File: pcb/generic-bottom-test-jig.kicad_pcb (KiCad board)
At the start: 2 copper layers, 88.5 x 56.8 mm, 47 parts, among them CON1 BARREL_JACK, P1 CONN_01X06, P10 CONN_01X01, P11 CONN_01X01, P2 CONN_02X25, P3 CONN_01X04, P4 CONN_02X25, P5 CONN_01X16, P6 CONN_02X10, P7 CONN_01X01, P8 CONN_01X16, P9 CONN_01X01, Q1 Q_NMOS_GSD, SW1 Switch_SPDT_x2, SW2 SPST, U1 STMPS2151, U2 TLV70233DBV, U3 74LS257

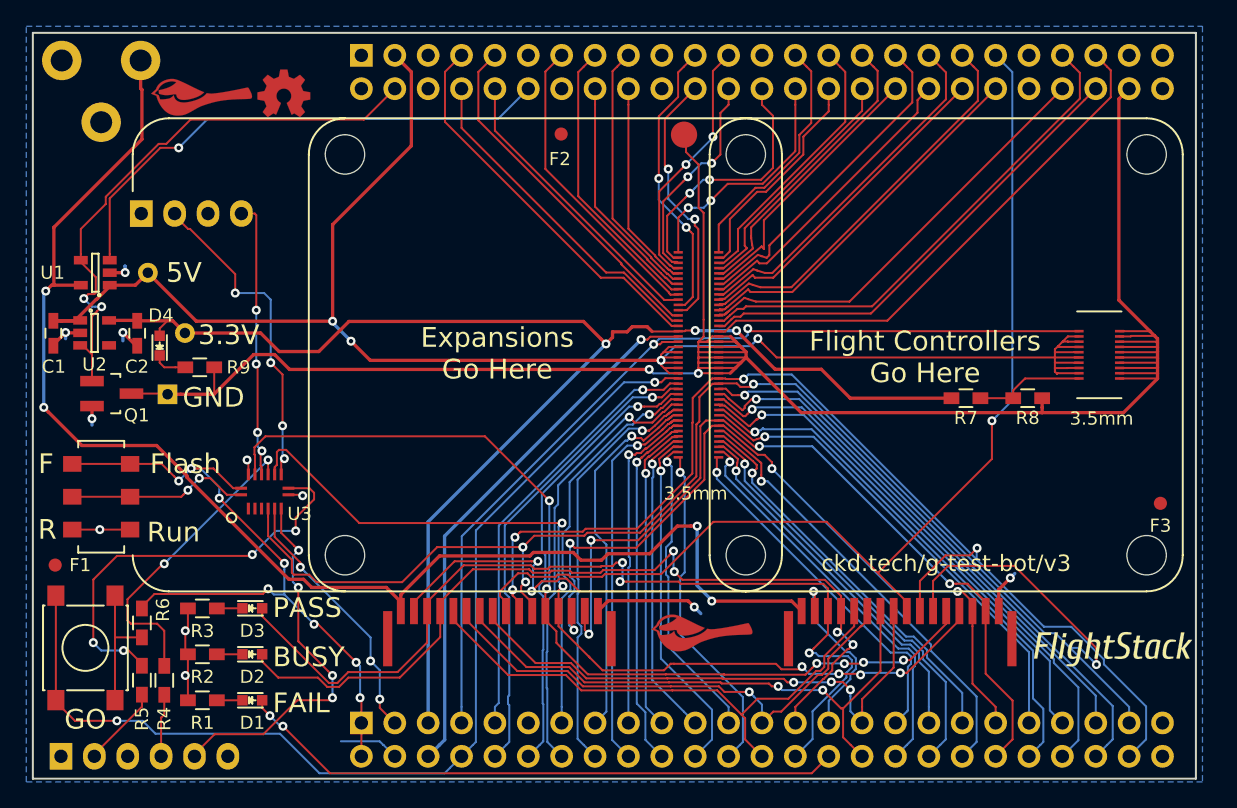
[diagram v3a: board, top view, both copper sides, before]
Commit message: Rebrand everything to Polystack and increment versions.
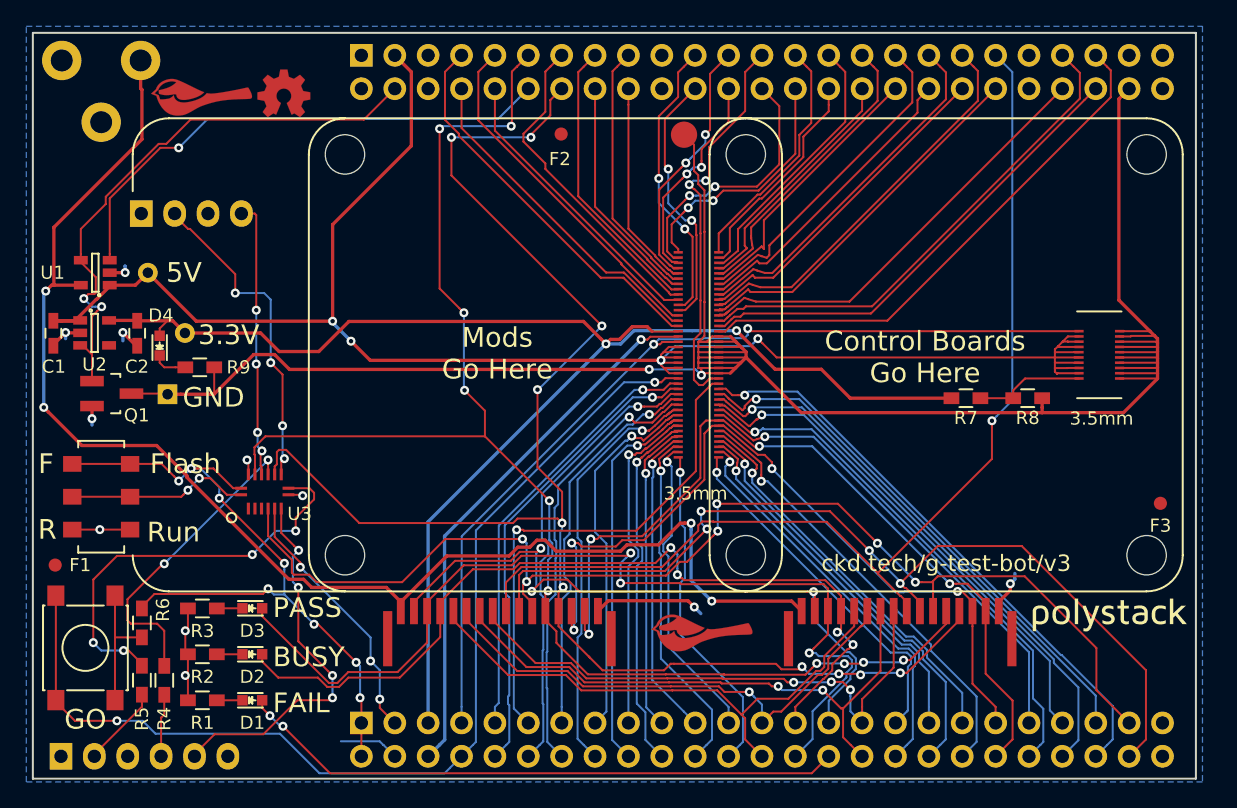
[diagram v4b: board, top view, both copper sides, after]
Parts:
- removed the G*** at (191.2, 130.4)
- added svg2mod: G***, polystack:polystack-medium-13mm, F.Cu at (190.9, 127.8)
- added svg2mod: G***, polystack:polystack-normal-0.625, B.Cu at (184.4, 106.3)
- added svg2mod: G***, polystack:polystack-normal-0.75, B.Cu at (183.2, 103.7)
- added svg2mod: G***, polystack:polystack-normal-1, B.Cu at (181.0, 100.3)
- added svg2mod: G***, polystack:polystack-normal-1.1, B.Cu at (180.1, 96.0)
- added svg2mod: G***, polystack:polystack-bold-1.1, B.Cu at (136.4, 96.0)
- added svg2mod: G***, polystack:polystack-bold-1, B.Cu at (137.6, 99.9)
- added svg2mod: G***, polystack:polystack-bold-0.75, B.Cu at (139.9, 103.3)
- added svg2mod: G***, polystack:polystack-bold-0.625, B.Cu at (141.2, 106.0)
- added svg2mod: G***, polystack:polystack-bold-0.5, B.Cu at (142.5, 108.5)
- added svg2mod: G***, polystack:polystack-bold-0.4, B.Cu at (142.8, 112.0)
- added svg2mod: G***, polystack:polystack-medium-1.1, B.Cu at (158.6, 96.0)
- added svg2mod: G***, polystack:polystack-medium-1, B.Cu at (159.5, 99.9)
- added svg2mod: G***, polystack:polystack-medium-0.75, B.Cu at (161.9, 103.5)
- added svg2mod: G***, polystack:polystack-medium-0.625, B.Cu at (171.2, 106.2)
- added svg2mod: G***, polystack:polystack-medium-0.5, B.Cu at (172.3, 108.5)
- added svg2mod: G***, polystack:polystack-medium-0.4, B.Cu at (173.3, 110.7)
- added svg2mod: G***, polystack:polystack-normal-0.4, B.Cu at (186.5, 110.8)
- added svg2mod: G***, polystack:polystack-normal-0.5, B.Cu at (185.6, 108.8)
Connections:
- net /PE4 renamed /PE4_FAULT
- P2 pad 11: /PA0 -> /PA0_MEZ_RESET
- P4 pad 11: /PE5 -> /TEST_SWDIO
- P4 pad 14: /PE2 -> /TEST_SWCLK
- P4 pad 25: /PB3_SWO -> /PB3_SWO_MEZ_BOOT
- PORT_OUT1 pad 65: /PC6_BOOT0 -> /PB3_SWO_MEZ_BOOT
- PORT_OUT1 pad 66: /PC7_RESET -> /PA0_MEZ_RESET
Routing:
- net /TEST_SWCLK: track 69.3 -> 117.1 mm, vias 6 -> 10
- net /PA0_MEZ_RESET: track 0.00 -> 38.5 mm, vias 0 -> 1
- net /TEST_SWDIO: track 71.4 -> 107.9 mm, vias 6 -> 10
- net /PB3_SWO_MEZ_BOOT: track 0.00 -> 30.4 mm, vias 0 -> 2
- net /PC7_RESET: track 117.9 -> 92.0 mm, vias 4 -> 6
- net /PC6_BOOT0: track 86.0 -> 71.2 mm
- net /PC0_3V3: track 106.1 -> 111.7 mm, vias 3 -> 2
- net /PE11_LD7_GREEN: track 71.6 -> 73.3 mm
- net /PE12_LD9_BLUE: track 50.0 -> 51.6 mm
- net /PE3: track 23.3 -> 24.6 mm
- net +5V: track 105.5 -> 104.8 mm
- net /PD5: track 18.4 -> 18.9 mm
- net /PA6_SDO: track 25.1 -> 25.6 mm
- net /PC8_GND: track 181.4 -> 181.9 mm
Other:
- rule pad_to_mask_clearance: 0.2 -> 0.0762
- board text added: ".4"
- board text added: ".5"
- board text added: ".625"
- board text added: ".75"
- board text added: "1.0"
- board text added: "1.1"
- board text added: "Bold"
- board text added: "Control Boards Go Here"
- board text added: "Medium"
- board text added: "Mods Go Here"
- board text added: "Regular"
- board text removed: "Expansions Go Here"
- board text removed: "Flight Controllers Go Here"
- board text removed: "This side intentionally left blank. (Its the back.)"

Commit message: Final gerbers for test manufacturing run.
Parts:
- removed the svg2mod at (190.9, 127.8)
- added svg2mod: G***, polystack:polystack-medium-0.625, F.Cu at (190.9, 127.8)
- CON1: footprint barrel-jack:PJ-037BH-SMT -> barrel-jack:PJ-037BH-SMT-OVAL-EDGE
- moved P5 0.90 mm to (144.5, 129.1)
- moved P8 0.90 mm to (175.0, 129.1)
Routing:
- net GND: track 38.7 -> 52.5 mm, vias 11 -> 13
- net +5V: track 104.8 -> 108.5 mm, vias 4 -> 5
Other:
- outline, holes or cut-outs redrawn
- board text added: "Mod your STM32F3Discovery at your own risk!"
- board text added: "Remove both buttons (cutting them off is easiest). Remove U3 and U5 or cut all traces to them."
- board text added: "Replace SWD and Idd headers with males from below. Remove SB7."
- board text added: "Replace SWD jumper headers with males from below."
- board text added: "Silkscreen test above. Female pin headers should face this way to connect to modded STM32F3 Discovery."

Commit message: Remove polystack silkscreen tests and add polystack.org URL.
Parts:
- removed the svg2mod at (184.4, 106.3)
- removed the svg2mod at (183.2, 103.7)
- removed the svg2mod at (181.0, 100.3)
- removed the svg2mod at (180.1, 96.0)
- removed the svg2mod at (136.4, 96.0)
- removed the svg2mod at (137.6, 99.9)
- removed the svg2mod at (139.9, 103.3)
- removed the svg2mod at (141.2, 106.0)
- removed the svg2mod at (142.5, 108.5)
- removed the svg2mod at (142.8, 112.0)
- removed the svg2mod at (158.6, 96.0)
- removed the svg2mod at (159.5, 99.9)
- removed the svg2mod at (161.9, 103.5)
- removed the svg2mod at (171.2, 106.2)
- removed the svg2mod at (172.3, 108.5)
- removed the svg2mod at (173.3, 110.7)
- removed the svg2mod at (186.5, 110.8)
- removed the svg2mod at (185.6, 108.8)
- added svg2mod: G***, polystack:polystack-bold-0.75, F.Cu at (148.0, 103.5)
- added svg2mod: G***, polystack:polystack-bold-0.75, F.Cu at (178.5, 103.5)
- svg2mod: footprint polystack:polystack-medium-0.625 -> polystack:polystack-bold-0.625
- moved svg2mod 0.22 mm to (191.2, 127.7)
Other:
- board text added: "Female pin headers should face this way to connect to modded STM32F3 Discovery."
- board text added: "See ckd.tech/g-test-bot/v4 and polystack.org for latest info."
- board text added: "ckd.tech/g-test-bot/v4"
- board text removed: ".4"
- board text removed: ".5"
- board text removed: ".625"
- board text removed: ".75"
- board text removed: "1.0"
- board text removed: "1.1"
- board text removed: "Bold"
- board text removed: "Medium"
- board text removed: "Regular"
- board text removed: "Silkscreen test above. Female pin headers should face this way to connect to modded STM32F3 Discovery."
- board text removed: "ckd.tech/g-test-bot/v3"

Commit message: Add license information to many files. PCB design files are CC-BY and code is MIT license.
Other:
- board text added: "Copyright 2016 Chickadee Tech LLC, <add attributions here> This work is licensed under the Creative Commons Attribution 4.0 International License. To view a copy of this license, visit http://creativecommons.org/licenses/by/4.0/ or send a letter to Creative Commons, PO Box 1866, Mountain View, CA 94042, USA."
- board text added: "Remove all Chickadee Tech LLC trademarks before making your own board. The Chickadee logo and Polystack logo are owned by Chickadee Tech LLC. You may license the Polystack logo for free by emailing support@chickadee.tech and receiving express written permission from Chickadee Tech LLC."
- board text added: "The gear logo is a mark designating open source hardware. Remove it if your design does not comply with the open source hardware definition."
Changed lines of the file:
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@@
     (area 103.275139 74.1 282.738096 178)
     (thickness 1.6)
-    (drawings 74)
+    (drawings 81)
     (tracks 1827)
     (zones 0)
@@
     (40 Dwgs.User user)
     (41 Cmts.User user)
-    (42 Eco1.User user hide)
-    (43 Eco2.User user hide)
+    (42 Eco1.User user)
+    (43 Eco2.User user)
     (44 Edge.Cuts user)
     (45 Margin user)
@@
       (xy 4.672239 0.694521)) (layer F.SilkS) (width 0))
   )
+  (gr_line (start 190.51 128.79) (end 124.54 145.9) (layer Cmts.User) (width 0.15))
+  (gr_line (start 124.2 146.13) (end 122.51 90.96) (layer Cmts.User) (width 0.15))
+  (gr_line (start 156.55 130.53) (end 124.2 146.13) (layer Cmts.User) (width 0.15))
+  (gr_text "Remove all Chickadee Tech LLC trademarks\nbefore making your own board. The\nChickadee logo and Polystack logo\nare owned by Chickadee Tech LLC.\n\nYou may license the Polystack logo for\nfree by emailing support@chickadee.tech\nand receiving express written permission\nfrom Chickadee Tech LLC." (at 103.05 157.33) (layer Cmts.User)
+    (effects (font (size 1.5 1.5) (thickness 0.3)) (justify left))
+  )
+  (gr_line (start 128.1 85.46) (end 122.43 66.56) (layer Cmts.User) (width 0.15))
+  (gr_text "The gear logo is a mark designating open\nsource hardware. Remove it if your design\ndoes not comply with the open source\nhardware definition." (at 100.47 61.61) (layer Cmts.User)
+    (effects (font (size 1.5 1.5) (thickness 0.3)) (justify left))
+  )
+  (gr_text "Copyright 2016 Chickadee Tech LLC, <add attributions here>\n\nThis work is licensed under the Creative Commons Attribution 4.0 International License.\nTo view a copy of this license, visit http://creativecommons.org/licenses/by/4.0/\nor send a letter to Creative Commons, PO Box 1866, Mountain View, CA 94042, USA." (at 178.67 174.2) (layer Cmts.User)
+    (effects (font (size 1.5 1.5) (thickness 0.3)) (justify left))
+  )
   (gr_text "See ckd.tech/g-test-bot/v4\nand polystack.org for latest\ninfo." (at 195.52 116.83) (layer B.SilkS)
     (effects (font (size 1.25 1.25) (thickness 0.22)) (justify left mirror))
@@
   (gr_line (start 166 92.75) (end 166 123.25) (angle 90) (layer F.SilkS) (width 0.15))
   (gr_line (start 119.35 90) (end 163.25 90) (angle 90) (layer F.SilkS) (width 0.15))
-  (gr_text generic-bottom-test-jig (at 187.25 174.25) (layer Cmts.User)
-    (effects (font (size 5 5) (thickness 0.5)) (justify left))
+  (gr_text generic-bottom-test-jig (at 186.14 189.73) (layer Cmts.User)
+    (effects (font (size 3 3) (thickness 0.5)) (justify left))
   )
   (segment (start 158.5 91.2) (end 158.55 91.25) (width 0.1524) (layer B.Cu) (net 0))
